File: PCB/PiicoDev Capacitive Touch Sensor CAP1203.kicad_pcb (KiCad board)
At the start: 2 copper layers, 25.4 x 52 mm, 44 parts, among them J1 , J11 Conn_01x01_Male, J12 Conn_01x01_Male, J13 Conn_01x01_Male, J2 , J3 Conn_PiicoDev_header_01x04_Ma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, J4 Conn_01x01_Male, J5 Conn_01x01_Male, J6 Conn_01x01_Male, J7 Conn_01x01_Male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

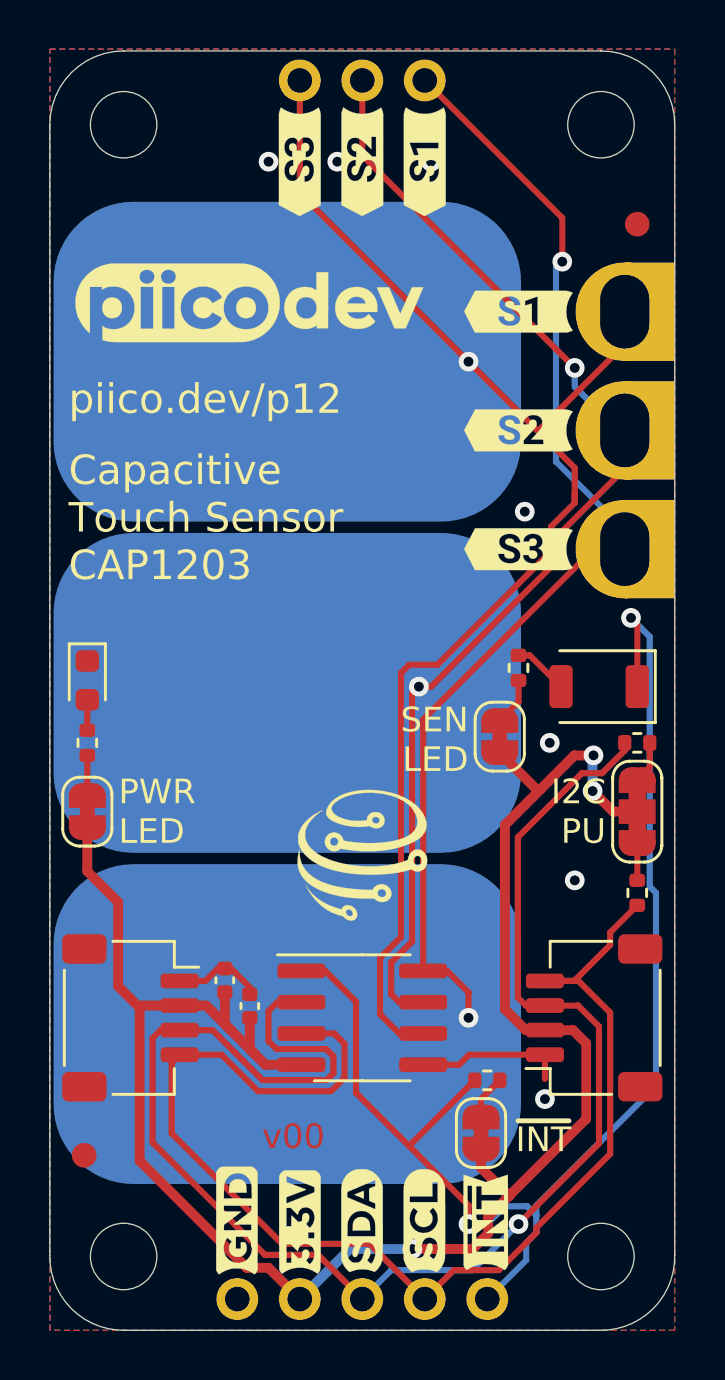
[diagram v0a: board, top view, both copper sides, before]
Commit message: Update interrupt LED and increase alligator clip hole size
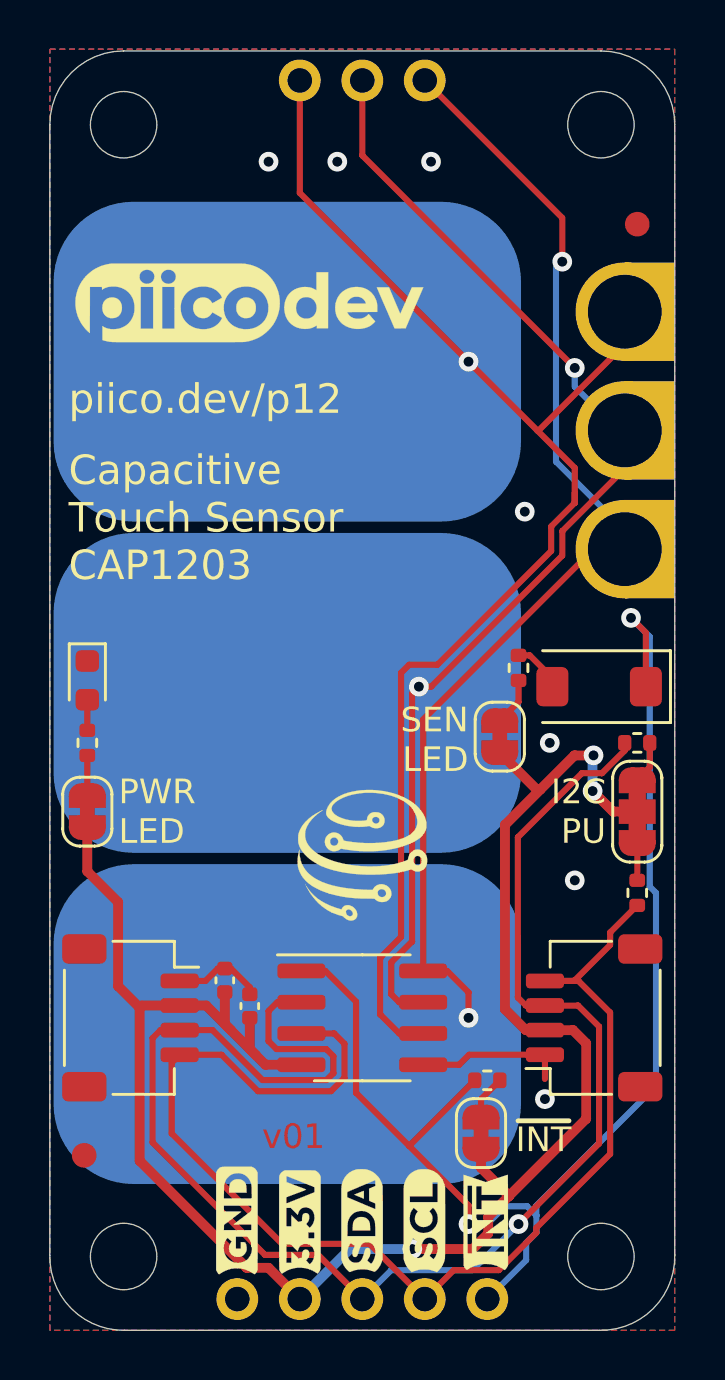
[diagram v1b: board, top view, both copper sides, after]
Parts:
- removed the G*** at (103.6, 82.3)
- removed the G*** at (103.6, 77.5)
- removed the G*** at (103.6, 72.6)
- removed the G*** at (97.3, 66.5)
- removed the G*** at (99.8, 66.5)
- removed the G*** at (94.7, 66.5)
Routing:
- net /~INT: track 54.5 -> 55.0 mm
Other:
- board text added: "v01"
- board text removed: "v00"

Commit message: Add silk screen labels
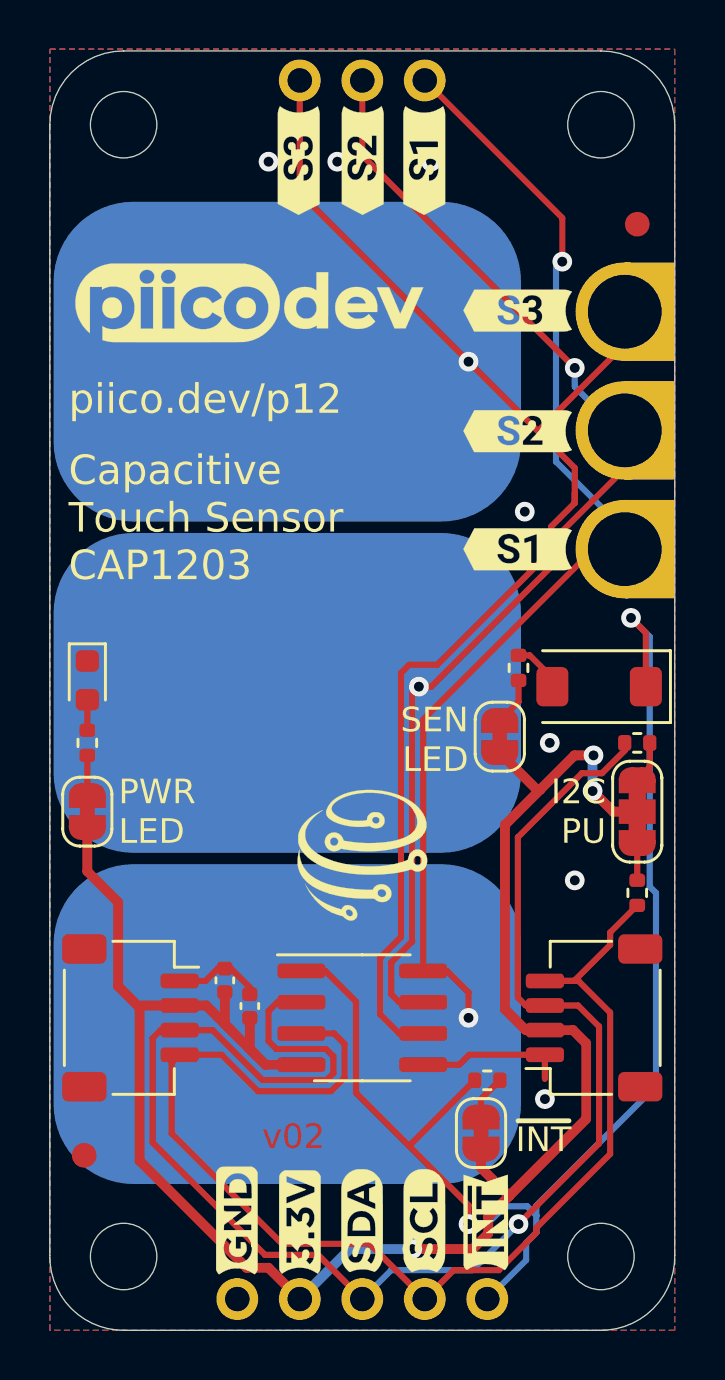
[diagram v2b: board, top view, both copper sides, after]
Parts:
- added G4: S1, PiicoDev Capacitive Touch Sensor CAP1203:Label_S1_Reverse, F.Cu at (99.8, 66.5)
- added G5: S1, PiicoDev Capacitive Touch Sensor CAP1203:Label_S1_Reverse, F.Cu at (103.6, 82.3)
- added G6: S2, PiicoDev Capacitive Touch Sensor CAP1203:Label_S2_Reverse, F.Cu at (97.3, 66.5)
- added G7: S2, PiicoDev Capacitive Touch Sensor CAP1203:Label_S2_Reverse, F.Cu at (103.6, 77.5)
- added G8: S3, PiicoDev Capacitive Touch Sensor CAP1203:Label_S3_Reverse, F.Cu at (94.7, 66.5)
- added G9: S3, PiicoDev Capacitive Touch Sensor CAP1203:Label_S3_Reverse, F.Cu at (103.6, 72.6)
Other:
- board text added: "v02"
- board text removed: "v01"

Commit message: Increase Alligator Clip Size
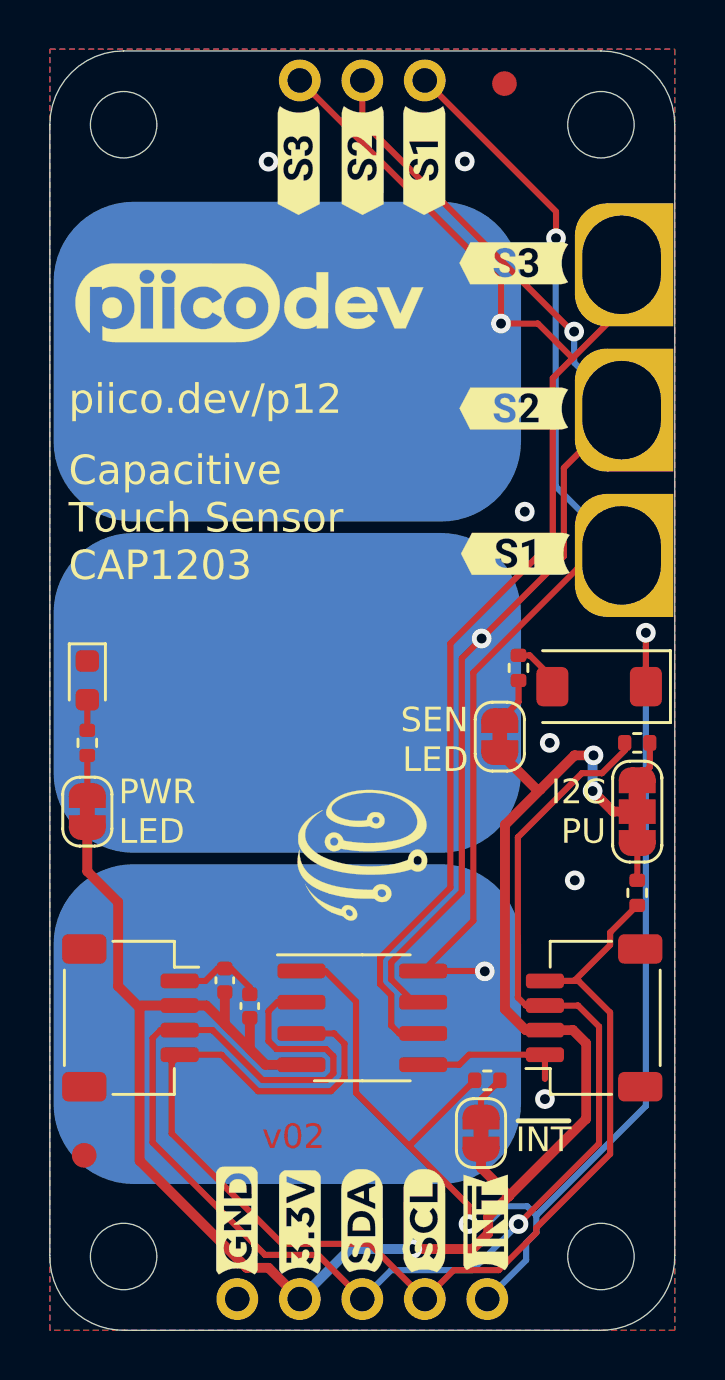
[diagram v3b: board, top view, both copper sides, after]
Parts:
- J11, J12, J13: footprint CoreElectronics_Components:Conn_alligator-banana_small -> CoreElectronics_Components:Conn_alligator
- moved FID2 7.86 mm to (103.1, 63.4)
- moved G9 1.93 mm to (103.4, 70.7)
- moved J13 1.91 mm to (107.8, 70.7)
- moved G7 0.93 mm to (103.4, 76.6)
- moved J12 0.84 mm to (107.8, 76.6)
- moved J11 0.28 mm to (107.8, 82.5)
- moved G5 0.21 mm to (103.5, 82.5)
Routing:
- net /~INT: track 55.0 -> 52.6 mm
- net /CS3: track 55.3 -> 53.4 mm
- net /CS1: track 46.9 -> 45.9 mm
- net GND: vias 7 -> 6

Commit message: Change top copper fill from grounded to floating sections
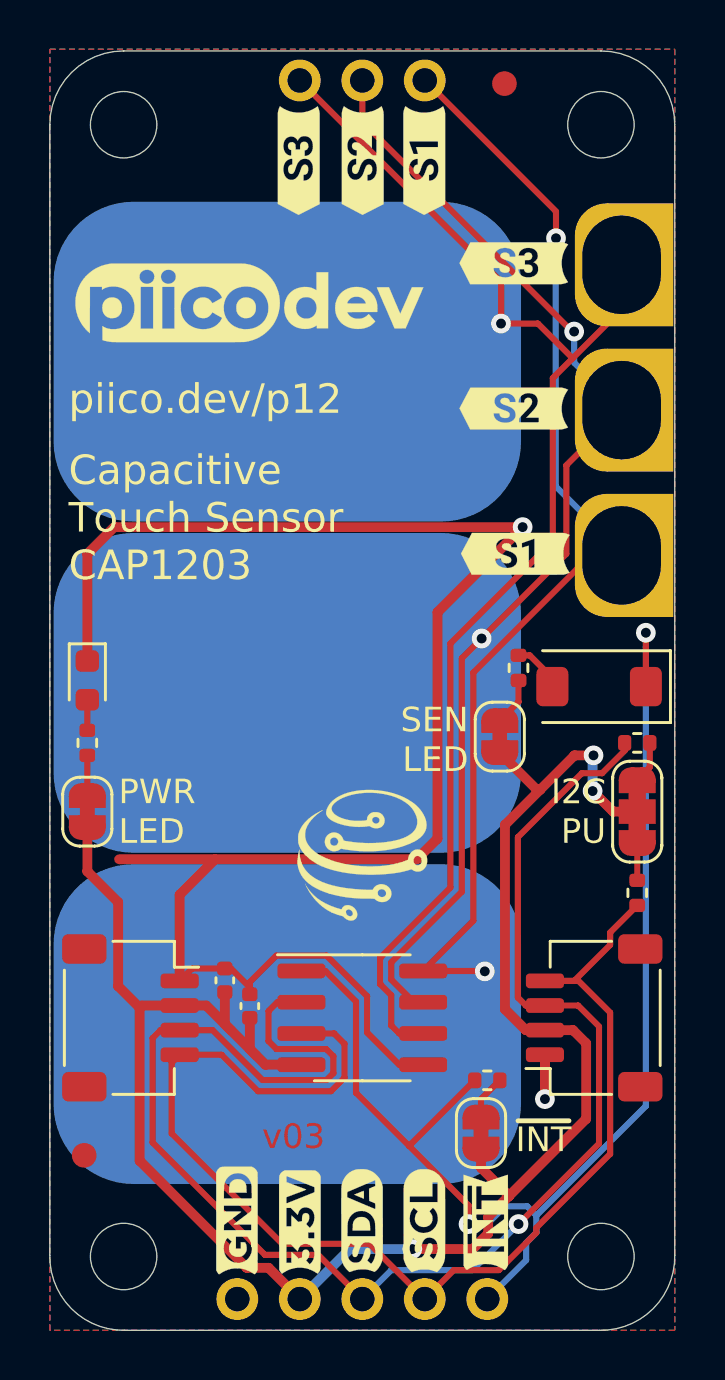
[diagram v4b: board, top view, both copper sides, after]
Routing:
- net GND: track 9.76 -> 72.9 mm, vias 6 -> 2
- added copper zone on F.Cu, net (none)
- removed copper zone on F.Cu, net GND
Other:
- board text added: "v03"
- board text removed: "v02"

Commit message: Revert "Change top copper fill from grounded to floating sections"
This reverts commit 368bc0d4ff66a5d992a58d852e4a1f950c0b97f4.
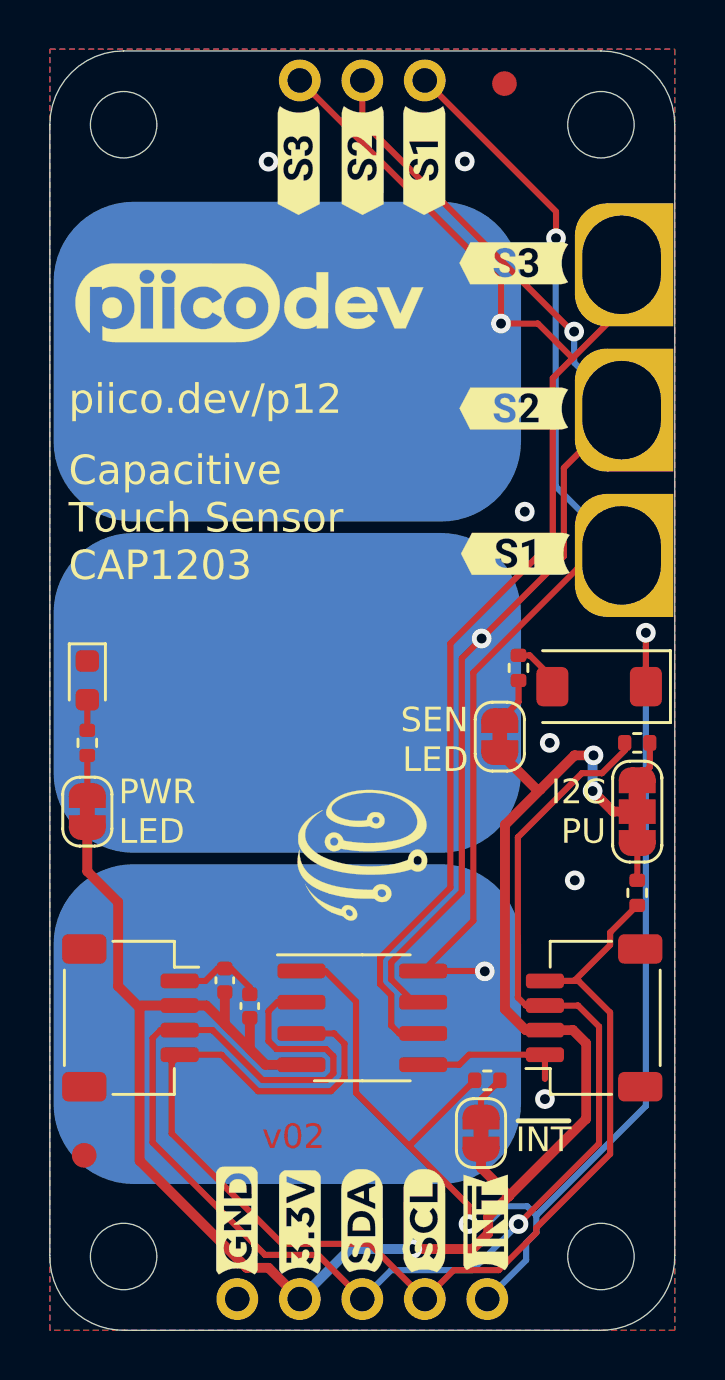
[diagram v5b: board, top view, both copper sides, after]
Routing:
- net GND: track 72.9 -> 9.76 mm, vias 2 -> 6
- added copper zone on F.Cu, net GND
- removed copper zone on F.Cu, net (none)
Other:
- board text added: "v02"
- board text removed: "v03"

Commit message: Update version number for production
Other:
- board text added: "v10"
- board text removed: "v02"

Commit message: Update R1,2,3,4 to 10k
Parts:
- R1: value 1k -> 10k
- R2, R3, R4: value 4k7 -> 10k

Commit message: Update user drawings - dimensioning
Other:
- board text added: "4x M2.5 (2.7mm) holes 1.2mm pad clearance"
- board text removed: "2x M2.5 (2.7mm) holes 1.2mm pad clearance"
